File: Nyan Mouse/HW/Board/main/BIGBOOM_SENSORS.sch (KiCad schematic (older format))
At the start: 31 parts, among them Q501 MOS_N, Q502 MOS_N, Q503 MOS_N, Q504 MOS_N, Q505 MOS_N, Q506 MOS_N, U501 74HC595

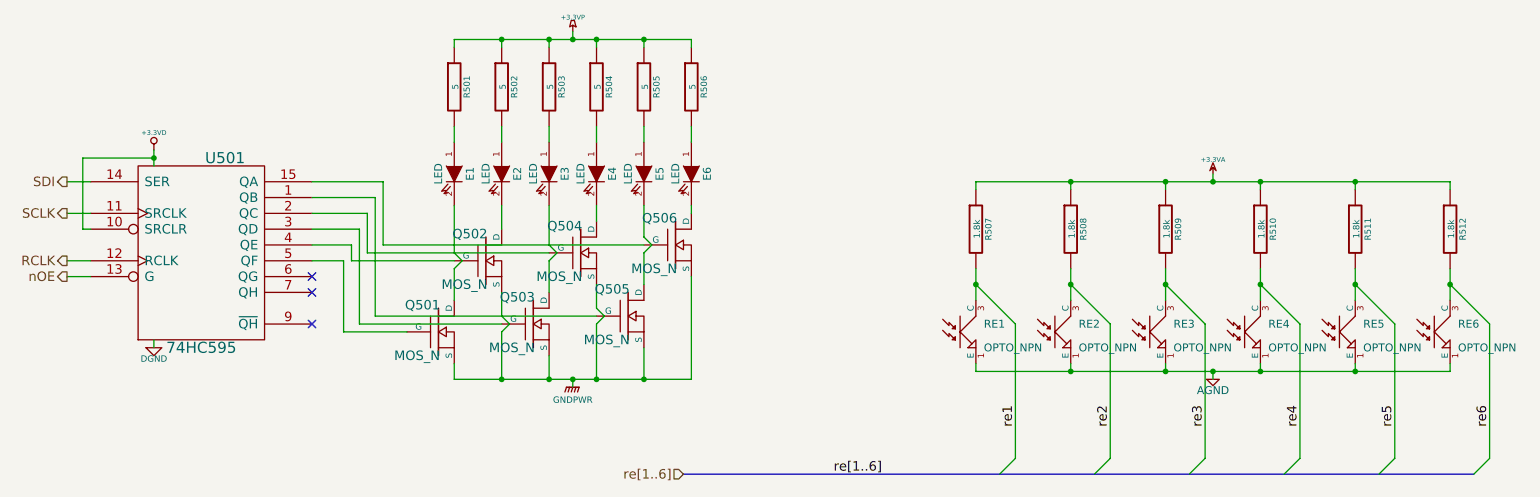
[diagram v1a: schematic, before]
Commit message: Flipped some RGB leds, added emitter pulldowns
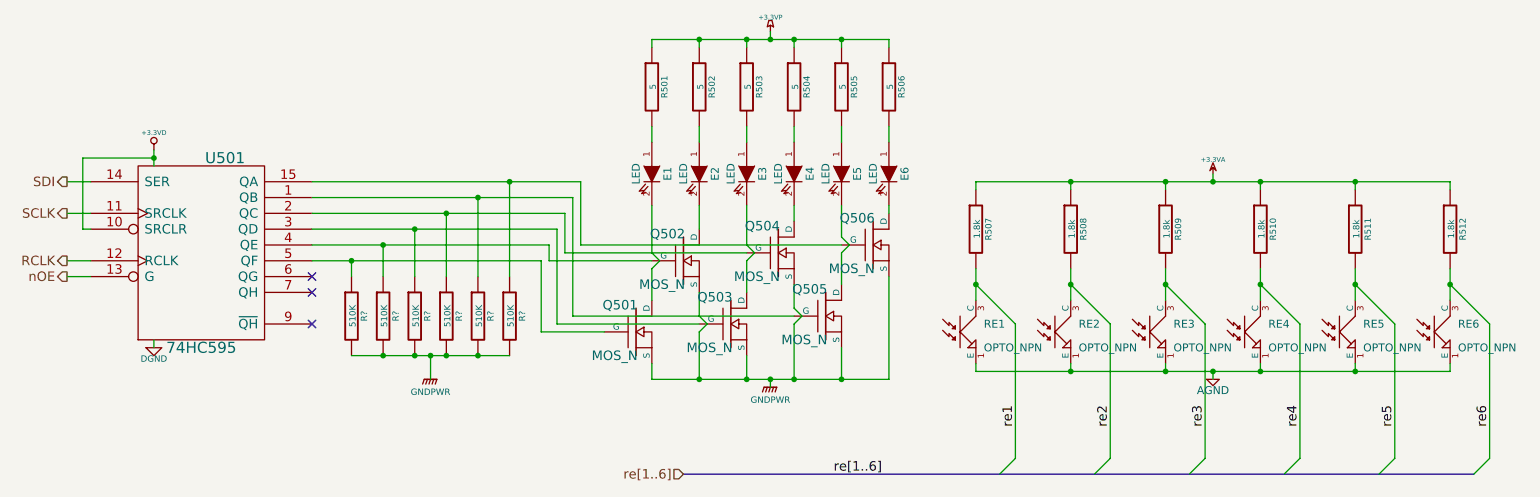
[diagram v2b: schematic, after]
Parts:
- added R? (x6): 510K, symbol R
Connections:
- net GNDPWR: now also R?.2, R?.2, R?.2, R?.2, R?.2, R?.2
- net at Q506.G, U501.15 (QA): now also R?.1
- net at Q504.G, U501.2 (QC): now also R?.1
- net at Q502.G, U501.4 (QE): now also R?.1
- net at Q505.G, U501.1 (QB): now also R?.1
- net at Q503.G, U501.3 (QD): now also R?.1
- net at Q501.G, U501.5 (QF): now also R?.1
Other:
- moved on the sheet: E1, E2, E3, E4, E5, E6, Q501, Q502, Q503, Q504, Q505, Q506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

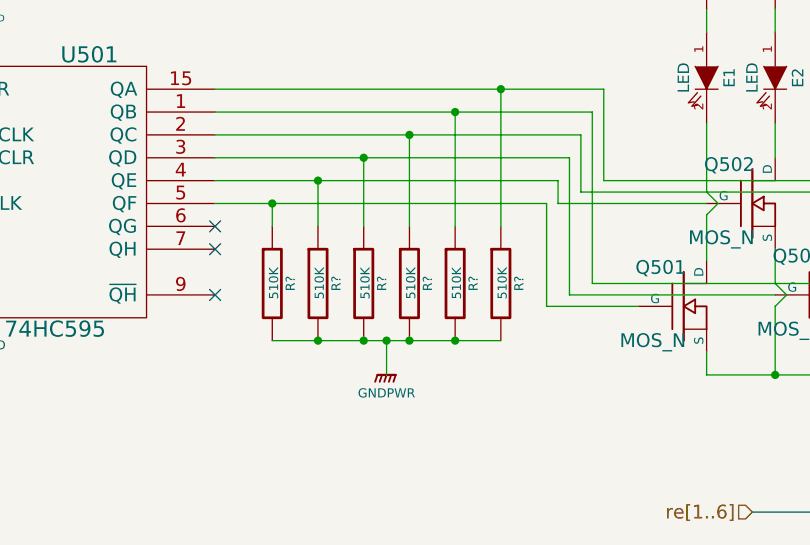
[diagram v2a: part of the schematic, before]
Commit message: Added bank names to FPGA
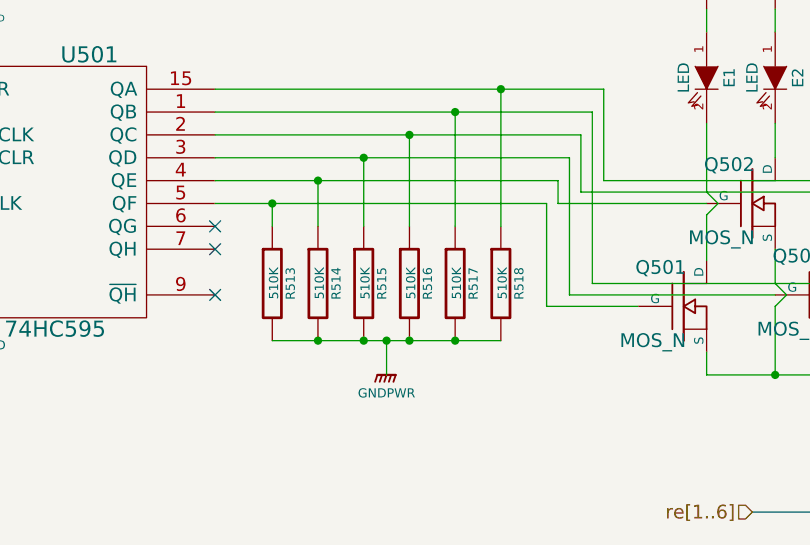
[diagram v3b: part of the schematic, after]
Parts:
- gave numbers to parts that had none: 6
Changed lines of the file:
@@
 LIBS:valves
 LIBS:Nyan Mouse-cache
-EELAYER 27 0
+EELAYER 24 0
 EELAYER END
 $Descr USLetter 11000 8500
@@
 $EndComp
 $Comp
-L GNDPWR #PWR056
+L GNDPWR #PWR505
 U 1 1 5357BFB1
 P 5300 2950
-F 0 "#PWR056" H 5300 3000 40  0001 C CNN
+F 0 "#PWR505" H 5300 3000 40  0001 C CNN
 F 1 "GNDPWR" H 5300 2870 40  0000 C CNN
 F 2 "" H 5300 2950 60  0000 C CNN
@@
 SCLK
 $Comp
-L DGND #PWR057
+L DGND #PWR502
 U 1 1 5357DEDF
 P 1400 2700
-F 0 "#PWR057" H 1400 2700 40  0001 C CNN
+F 0 "#PWR502" H 1400 2700 40  0001 C CNN
 F 1 "DGND" H 1400 2630 40  0000 C CNN
 F 2 "" H 1400 2700 60  0000 C CNN
@@
 $EndComp
 $Comp
-L +3.3VD #PWR058
+L +3.3VD #PWR501
 U 1 1 5357DEF3
 P 1400 1450
-F 0 "#PWR058" H 1400 1410 30  0001 C CNN
+F 0 "#PWR501" H 1400 1410 30  0001 C CNN
 F 1 "+3.3VD" H 1400 1560 30  0000 C CNN
 F 2 "" H 1400 1450 60  0000 C CNN
@@
 $EndComp
 $Comp
-L +3.3VP #PWR059
+L +3.3VP #PWR504
 U 1 1 5358178D
 P 5300 700
-F 0 "#PWR059" H 5350 730 20  0001 C CNN
+F 0 "#PWR504" H 5350 730 20  0001 C CNN
 F 1 "+3.3VP" H 5300 790 30  0000 C CNN
 F 2 "" H 5300 700 60  0000 C CNN
@@
 $EndComp
 $Comp
-L +3.3VA #PWR060
+L +3.3VA #PWR506
 U 1 1 5358765E
 P 8100 1600
-F 0 "#PWR060" H 8100 1720 20  0001 C CNN
+F 0 "#PWR506" H 8100 1720 20  0001 C CNN
 F 1 "+3.3VA" H 8100 1690 30  0000 C CNN
 F 2 "" H 8100 1600 60  0000 C CNN
@@
 $EndComp
 $Comp
-L AGND #PWR061
+L AGND #PWR507
 U 1 1 535876B6
 P 8100 2900
-F 0 "#PWR061" H 8100 2900 40  0001 C CNN
+F 0 "#PWR507" H 8100 2900 40  0001 C CNN
 F 1 "AGND" H 8100 2830 50  0000 C CNN
 F 2 "" H 8100 2900 60  0000 C CNN
@@
 re[1..6]
 $Comp
-L R R?
+L R R513
 U 1 1 53596F04
 P 2650 2500
-F 0 "R?" V 2730 2500 40  0000 C CNN
+F 0 "R513" V 2730 2500 40  0000 C CNN
 F 1 "510K" V 2657 2501 40  0000 C CNN
 F 2 "" V 2580 2500 30  0000 C CNN
@@
 $EndComp
 $Comp
-L R R?
+L R R514
 U 1 1 53596F10
 P 2850 2500
-F 0 "R?" V 2930 2500 40  0000 C CNN
+F 0 "R514" V 2930 2500 40  0000 C CNN
 F 1 "510K" V 2857 2501 40  0000 C CNN
 F 2 "" V 2780 2500 30  0000 C CNN
@@
 $EndComp
 $Comp
-L R R?
+L R R515
 U 1 1 53596F16
 P 3050 2500
-F 0 "R?" V 3130 2500 40  0000 C CNN
+F 0 "R515" V 3130 2500 40  0000 C CNN
 F 1 "510K" V 3057 2501 40  0000 C CNN
 F 2 "" V 2980 2500 30  0000 C CNN
@@
 $EndComp
 $Comp
-L R R?
+L R R516
 U 1 1 53596F1C
 P 3250 2500
-F 0 "R?" V 3330 2500 40  0000 C CNN
+F 0 "R516" V 3330 2500 40  0000 C CNN
 F 1 "510K" V 3257 2501 40  0000 C CNN
 F 2 "" V 3180 2500 30  0000 C CNN
@@
 $EndComp
 $Comp
-L R R?
+L R R517
 U 1 1 53596F22
 P 3450 2500
-F 0 "R?" V 3530 2500 40  0000 C CNN
+F 0 "R517" V 3530 2500 40  0000 C CNN
 F 1 "510K" V 3457 2501 40  0000 C CNN
 F 2 "" V 3380 2500 30  0000 C CNN
@@
 $EndComp
 $Comp
-L R R?
+L R R518
 U 1 1 535972CB
 P 3650 2500
-F 0 "R?" V 3730 2500 40  0000 C CNN
+F 0 "R518" V 3730 2500 40  0000 C CNN
 F 1 "510K" V 3657 2501 40  0000 C CNN
 F 2 "" V 3580 2500 30  0000 C CNN
@@
 $EndComp
 $Comp
-L GNDPWR #PWR?
+L GNDPWR #PWR503
 U 1 1 535972D1
 P 3150 2900
-F 0 "#PWR?" H 3150 2950 40  0001 C CNN
+F 0 "#PWR503" H 3150 2950 40  0001 C CNN
 F 1 "GNDPWR" H 3150 2820 40  0000 C CNN
 F 2 "" H 3150 2900 60  0000 C CNN
